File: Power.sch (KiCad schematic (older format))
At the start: 18 parts, among them Q100 AO3401A, U100 MP2359DJ-LF-Z

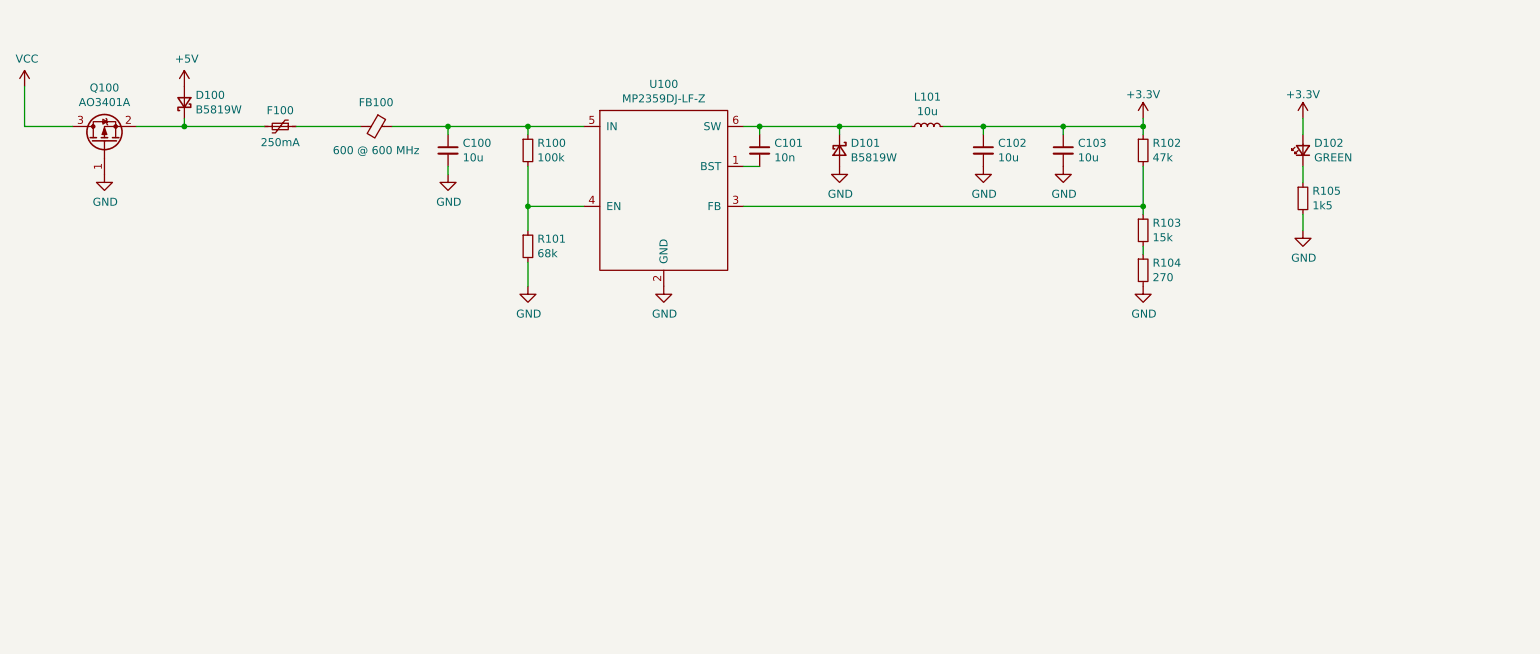
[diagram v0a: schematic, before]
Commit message: Updated firmware. Added schematic PDF.
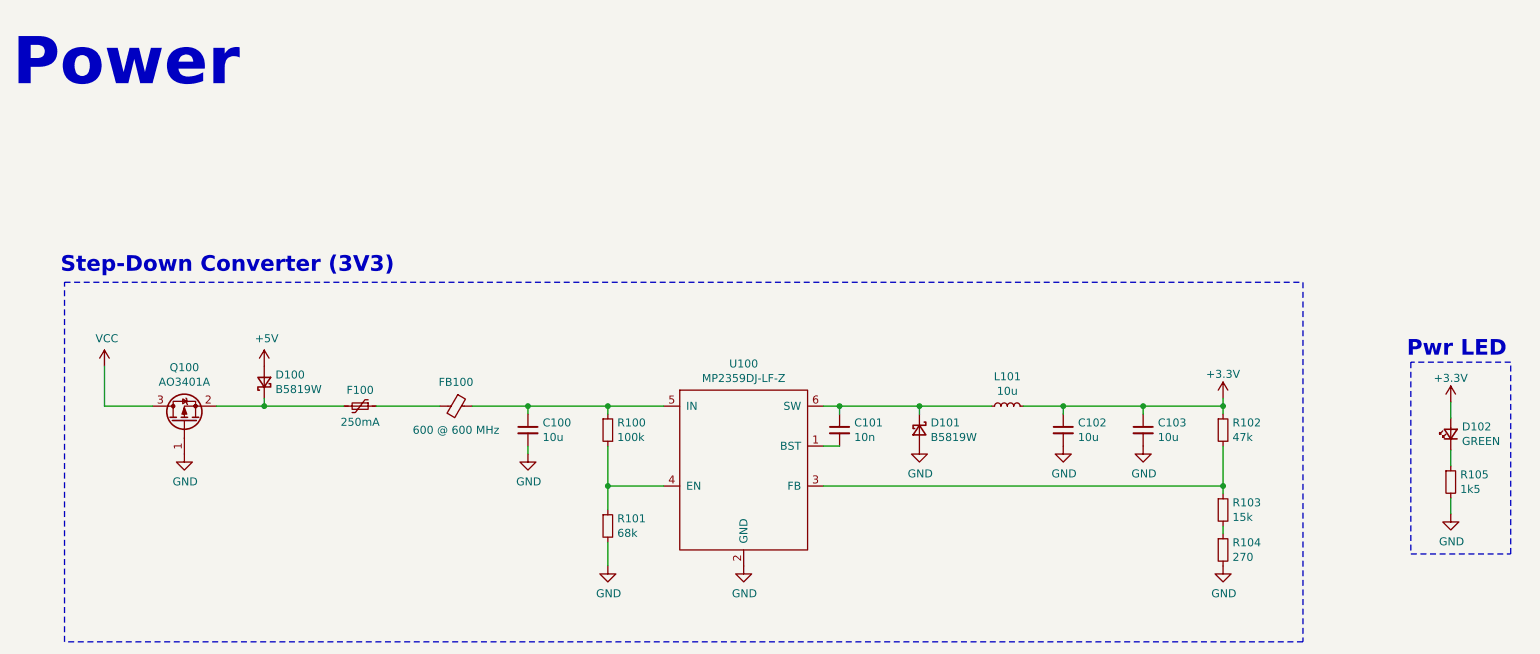
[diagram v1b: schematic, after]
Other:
- note added: "Power"
- note added: "Pwr LED"
- note added: "Step-Down Converter (3V3)"
- moved on the sheet: C100, C101, C102, C103, D100, D101, D102, F100, FB100, L101, Q100, R100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
